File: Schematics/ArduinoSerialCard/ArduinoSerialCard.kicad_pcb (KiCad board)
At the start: 2 copper layers, 50.8 x 27.9 mm, 2 parts, among them J1 Device 2

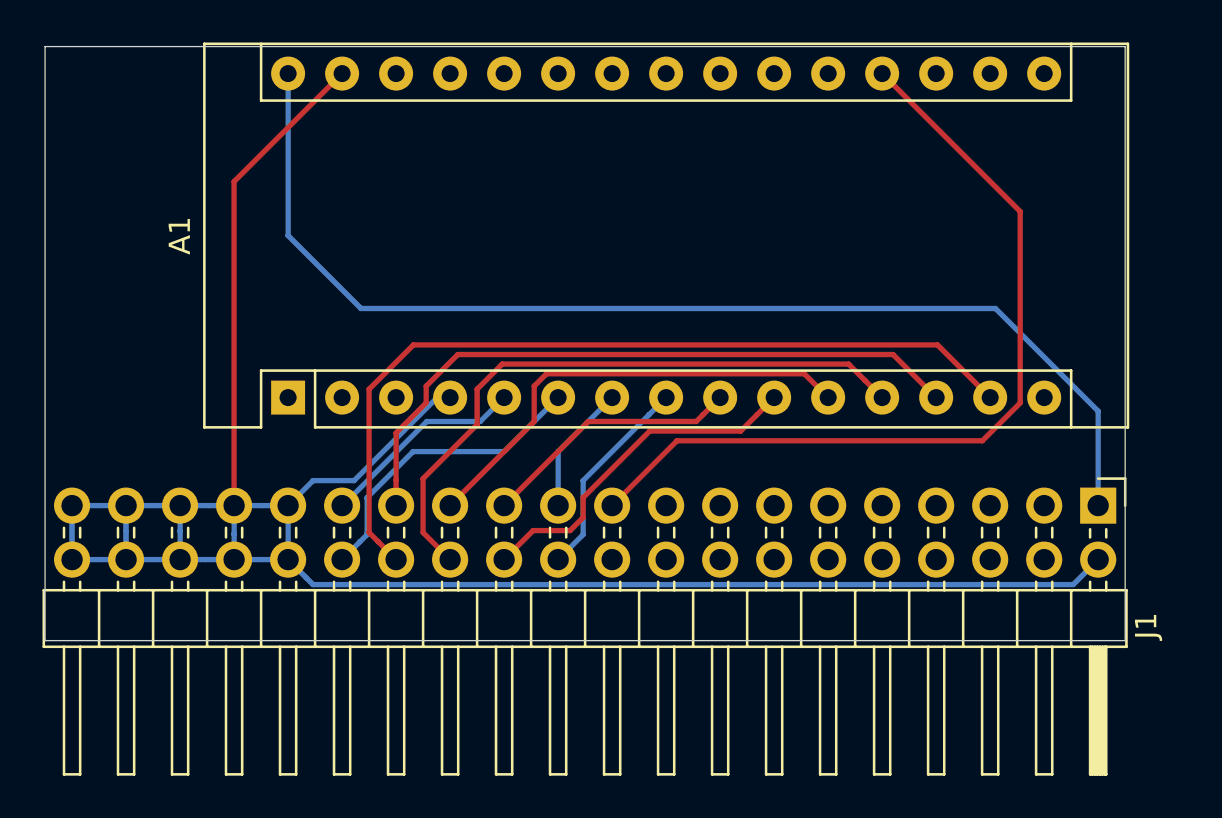
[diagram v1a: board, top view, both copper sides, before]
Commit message: Fix pin out on the Arduino Serial Card
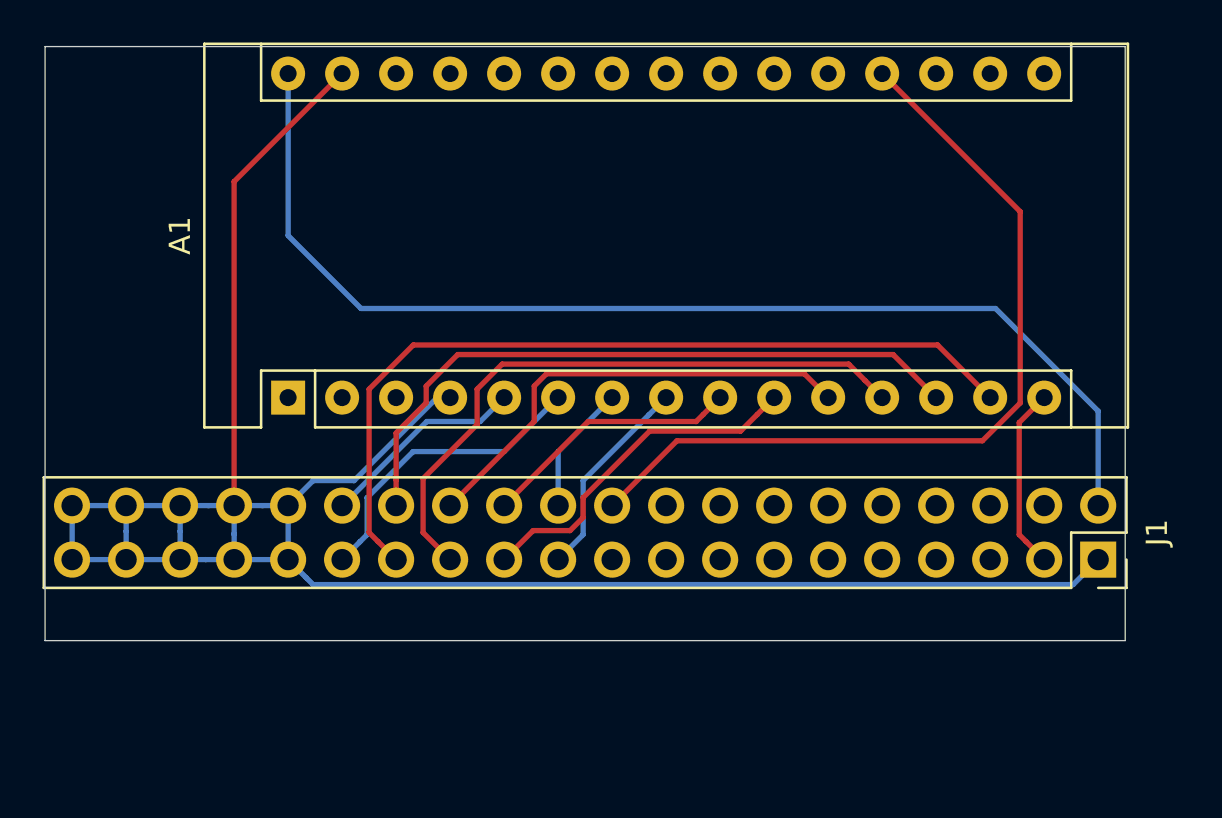
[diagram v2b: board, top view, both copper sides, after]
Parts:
- J1: value Device 2 -> Conn; footprint Connector_PinHeader_2.54mm:PinHeader_2x20_P2.54mm_Horizontal -> Connector_PinSocket_2.54mm:PinSocket_2x20_P2.54mm_Vertical
- moved J1 2.54 mm to (185.4, 81.3)
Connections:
- A1 pad 15: (no net) -> /AddressBus0
- A1 pad 16: /AddressBus0 -> (no net)
- A1 pad 19: /RegisterClock -> (no net)
- J1 pad 1: VCC -> GND
- J1 pad 10: (no net) -> Net-(J1-Pad10)
- J1 pad 11: (no net) -> Net-(J1-Pad11)
- J1 pad 12: (no net) -> Net-(J1-Pad12)
- J1 pad 13: (no net) -> Net-(J1-Pad13)
- J1 pad 14: (no net) -> Net-(J1-Pad14)
- J1 pad 15: (no net) -> Net-(J1-Pad15)
- J1 pad 16: (no net) -> Net-(J1-Pad16)
- J1 pad 17: (no net) -> Net-(J1-Pad17)
- J1 pad 18: (no net) -> Net-(J1-Pad18)
- J1 pad 19: /RegisterClock -> Net-(J1-Pad19)
- J1 pad 2: GND -> VCC
- J1 pad 20: (no net) -> Net-(J1-Pad20)
- J1 pad 4: (no net) -> Net-(J1-Pad4)
- J1 pad 5: (no net) -> Net-(J1-Pad5)
- J1 pad 6: (no net) -> Net-(J1-Pad6)
- J1 pad 7: (no net) -> Net-(J1-Pad7)
- J1 pad 8: (no net) -> Net-(J1-Pad8)
- J1 pad 9: (no net) -> Net-(J1-Pad9)
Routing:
- net /RegisterClock: track 39.4 -> 0.00 mm
- net (no net): track 0.00 -> 39.4 mm
- net /AddressBus0: track 0.00 -> 8.59 mm
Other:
- board text added: "Arduino Serial Interface © 2019 Andrew Fox, Rev 2"
- board text removed: "Arduino Serial Interface © 2019 Andrew Fox, Rev 1"

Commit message: Clean up the routing on the revised Serial Card PCB, and update generated files.
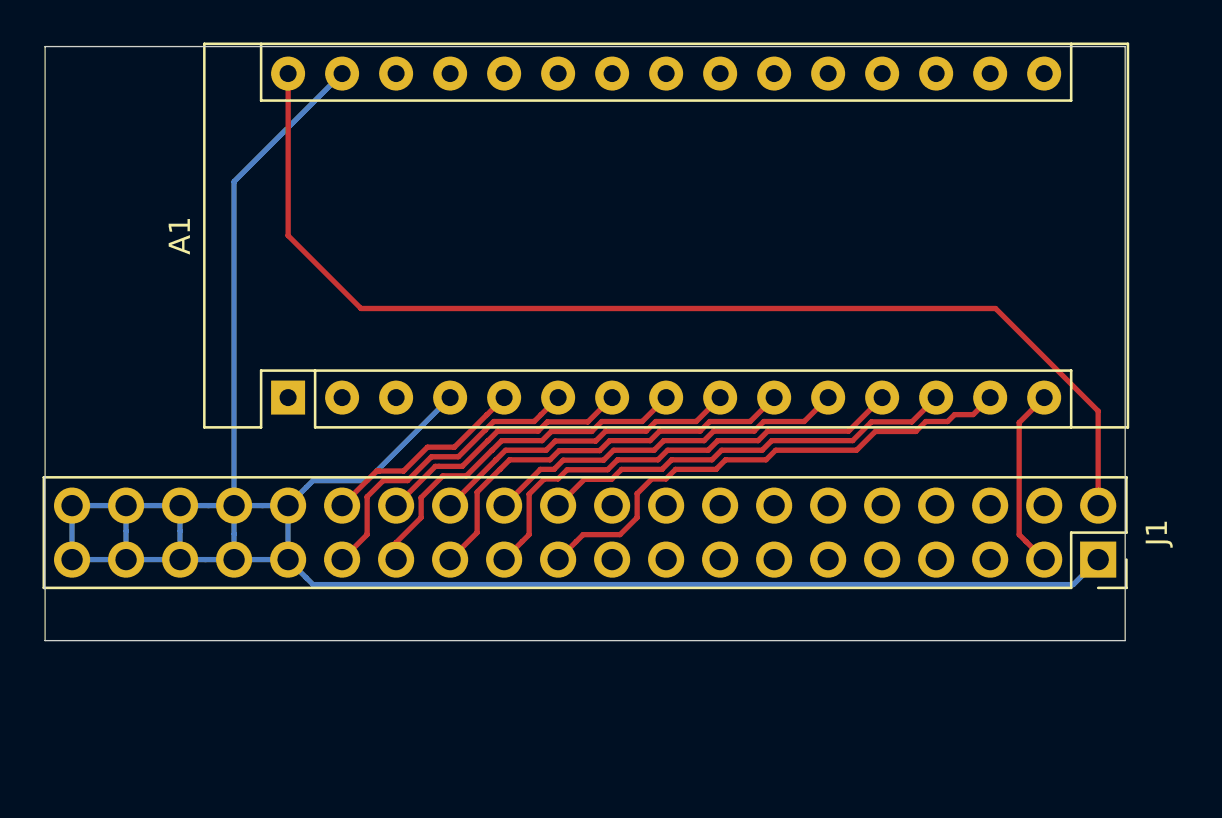
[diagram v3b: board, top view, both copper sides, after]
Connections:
- A1 pad 10: /DataBus3 -> /DataBus4
- A1 pad 11: /DataBus4 -> /DataBus3
- A1 pad 12: /DataBus5 -> /DataBus2
- A1 pad 13: /DataBus6 -> /DataBus1
- A1 pad 14: /DataBus7 -> /DataBus0
- A1 pad 5: /~PI -> /~PO
- A1 pad 6: /~PO -> /~PI
- A1 pad 7: /DataBus0 -> /DataBus7
- A1 pad 8: /DataBus1 -> /DataBus6
- A1 pad 9: /DataBus2 -> /DataBus5
- J1 pad 10: Net-(J1-Pad10) -> (no net)
- J1 pad 11: Net-(J1-Pad11) -> (no net)
- J1 pad 12: Net-(J1-Pad12) -> (no net)
- J1 pad 13: Net-(J1-Pad13) -> (no net)
- J1 pad 14: Net-(J1-Pad14) -> (no net)
- J1 pad 15: Net-(J1-Pad15) -> (no net)
- J1 pad 16: Net-(J1-Pad16) -> (no net)
- J1 pad 17: Net-(J1-Pad17) -> (no net)
- J1 pad 18: Net-(J1-Pad18) -> (no net)
- J1 pad 19: Net-(J1-Pad19) -> (no net)
- J1 pad 20: Net-(J1-Pad20) -> (no net)
- J1 pad 4: Net-(J1-Pad4) -> (no net)
- J1 pad 5: Net-(J1-Pad5) -> (no net)
- J1 pad 6: Net-(J1-Pad6) -> (no net)
- J1 pad 7: Net-(J1-Pad7) -> (no net)
- J1 pad 8: Net-(J1-Pad8) -> (no net)
- J1 pad 9: Net-(J1-Pad9) -> (no net)
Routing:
- net (no net): track 39.4 -> 0.00 mm
- net /DataBus7: track 39.6 -> 12.3 mm
- net /DataBus0: track 6.13 -> 24.1 mm
- net /DataBus5: track 29.8 -> 14.8 mm
- net /DataBus6: track 31.6 -> 16.9 mm
- net /DataBus1: track 9.72 -> 19.9 mm
- net /DataBus2: track 12.3 -> 22.1 mm
- net /~PI: track 9.72 -> 14.4 mm
- net /~PO: track 14.3 -> 9.72 mm
- net /DataBus4: track 21.8 -> 19.5 mm
- net /DataBus3: track 16.4 -> 17.3 mm
